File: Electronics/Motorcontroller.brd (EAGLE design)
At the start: 101.3 x 50.8 mm, 33 parts, among them Q1 IRFZ48V, Q2 IRF4905V, Q3 IRFZ48V, Q4 IRF4905V, Q5 IRFZ48V, Q6 IRF4905V, Q7 IRFZ48V, Q8 IRF4905V, X3 24V Batt

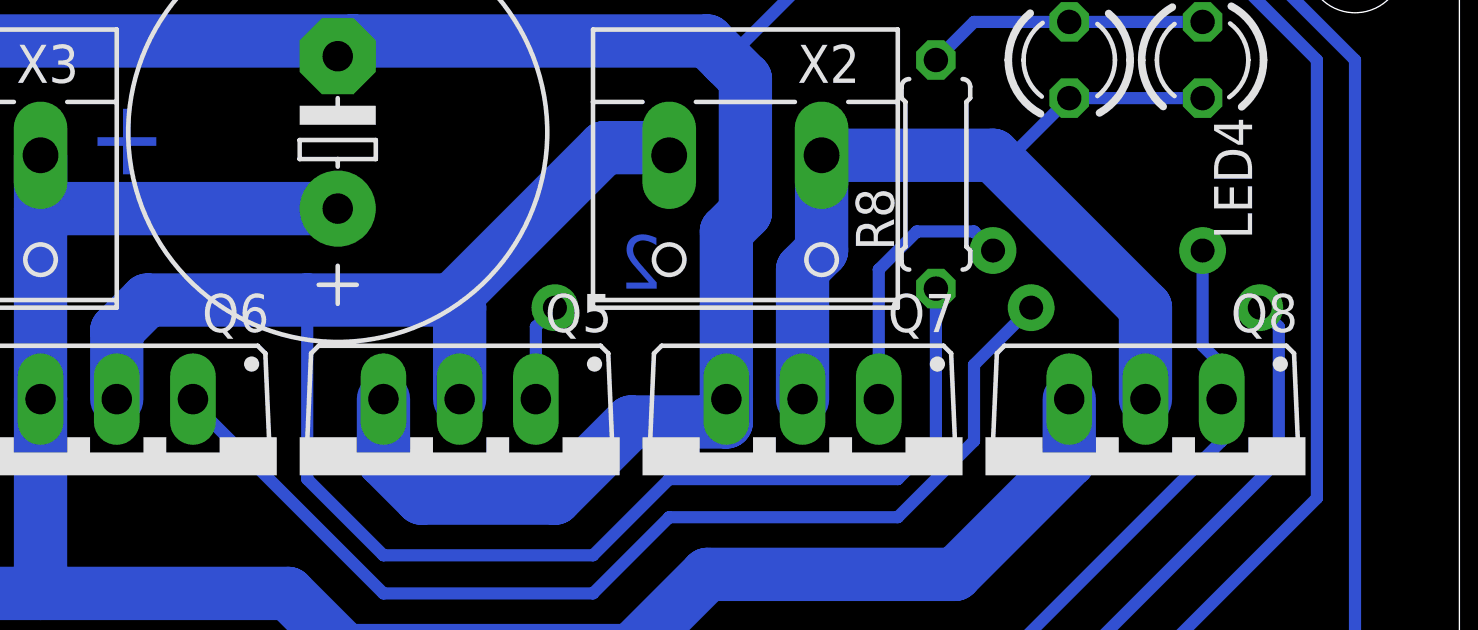
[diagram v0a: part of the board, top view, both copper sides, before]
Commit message: Renamed HEXFETs so both bridge fit
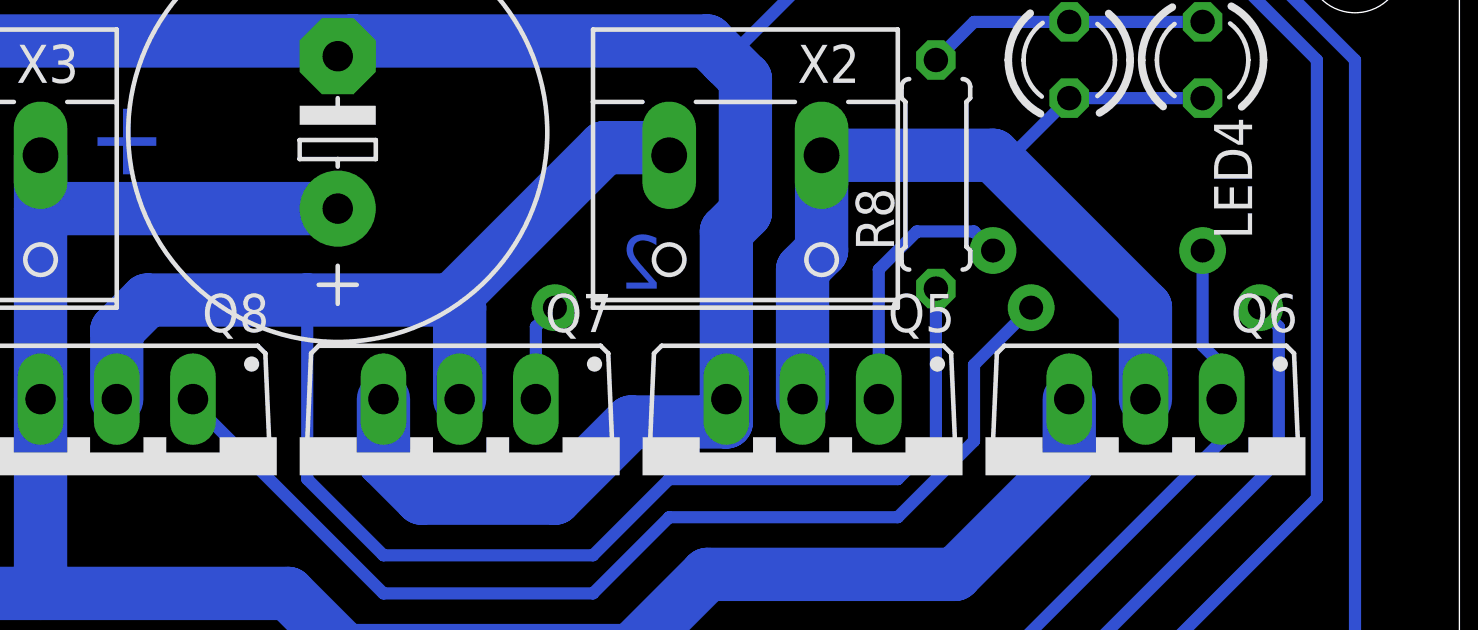
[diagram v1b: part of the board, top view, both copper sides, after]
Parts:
- moved Q6 34.3 mm to (90.2, 61.7)
- moved Q8 34.3 mm to (55.9, 61.7)
- moved Q5 11.4 mm to (78.7, 61.7)
- moved Q7 11.4 mm to (67.3, 61.7)
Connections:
- net N$1: now also Q5.D, Q6.D; no longer Q7.D, Q8.D
- net N$19: now also Q5.G, Q6.G; no longer Q7.G, Q8.G
- net N$21: now also Q8.G; no longer Q6.G
- net N$22: now also Q7.G; no longer Q5.G
- net N$25: now also Q7.D, Q8.D; no longer Q5.D, Q6.D
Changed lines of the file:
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@@
 <element name="R2" library="rcl" package="0207/10" value="10k" x="36.83" y="52.07" rot="R180"/>
 <element name="R3" library="rcl" package="0207/10" value="10k" x="50.8" y="52.07"/>
-<element name="Q5" library="transistor-power" package="TO220BV" value="IRFZ48V" x="67.31" y="61.722" rot="R180"/>
-<element name="Q6" library="transistor-power" package="TO220BV" value="IRF4905V" x="55.88" y="61.722" rot="R180"/>
+<element name="Q7" library="transistor-power" package="TO220BV" value="IRFZ48V" x="67.31" y="61.722" rot="R180"/>
+<element name="Q8" library="transistor-power" package="TO220BV" value="IRF4905V" x="55.88" y="61.722" rot="R180"/>
 <element name="X2" library="con-wago-508" package="W237-132" value="" x="76.835" y="71.755" rot="R180">
 <attribute name="OC_NEWARK" value="unknown" x="88.265" y="73.025" size="1.778" layer="27" rot="R180" display="off"/>
@@
 <attribute name="OC_FARNELL" value="unknown" x="88.265" y="73.025" size="1.778" layer="27" rot="R180" display="off"/>
 </element>
-<element name="Q7" library="transistor-power" package="TO220BV" value="IRFZ48V" x="78.74" y="61.722" rot="R180"/>
-<element name="Q8" library="transistor-power" package="TO220BV" value="IRF4905V" x="90.17" y="61.722" rot="R180"/>
+<element name="Q5" library="transistor-power" package="TO220BV" value="IRFZ48V" x="78.74" y="61.722" rot="R180"/>
+<element name="Q6" library="transistor-power" package="TO220BV" value="IRF4905V" x="90.17" y="61.722" rot="R180"/>
 <element name="R4" library="rcl" package="0207/10" value="10k" x="62.865" y="52.07" rot="R180"/>
 <element name="R5" library="rcl" package="0207/10" value="10k" x="75.565" y="52.07" rot="R180"/>
@@
 </signal>
 <signal name="N$19">
-<contactref element="Q8" pad="G"/>
-<contactref element="Q7" pad="G"/>
+<contactref element="Q6" pad="G"/>
+<contactref element="Q5" pad="G"/>
 <contactref element="R4" pad="1"/>
 <contactref element="OK4" pad="5"/>
@@
 </signal>
 <signal name="N$21">
-<contactref element="Q6" pad="G"/>
+<contactref element="Q8" pad="G"/>
 <contactref element="R5" pad="1"/>
 <contactref element="OK5" pad="5"/>
@@
 </signal>
 <signal name="N$22">
-<contactref element="Q5" pad="G"/>
+<contactref element="Q7" pad="G"/>
 <contactref element="R6" pad="1"/>
 <contactref element="OK6" pad="5"/>
@@
 </signal>
 <signal name="GND2">
+<contactref element="Q5" pad="S"/>
 <contactref element="Q7" pad="S"/>
-<contactref element="Q5" pad="S"/>
 <contactref element="X3" pad="2"/>
 <contactref element="Q3" pad="S"/>
@@
 <contactref element="Q4" pad="S"/>
 <contactref element="Q2" pad="S"/>
-<contactref element="Q6" pad="S"/>
+<contactref element="Q8" pad="S"/>
 <contactref element="R6" pad="2"/>
 <contactref element="R5" pad="2"/>
@@
 <contactref element="R2" pad="2"/>
 <contactref element="R1" pad="2"/>
-<contactref element="Q8" pad="S"/>
+<contactref element="Q6" pad="S"/>
 <contactref element="X3" pad="1"/>
 <wire x1="30.48" y1="64.262" x2="30.48" y2="60.96" width="1.778" layer="16"/>
@@
 </signal>
 <signal name="N$25">
-<contactref element="Q5" pad="D"/>
-<contactref element="Q6" pad="D"/>
+<contactref element="Q7" pad="D"/>
+<contactref element="Q8" pad="D"/>
 <contactref element="X2" pad="2"/>
 <wire x1="55.88" y1="64.262" x2="55.88" y2="66.548" width="1.778" layer="16"/>
@@
 <contactref element="LED4" pad="K"/>
 <contactref element="LED5" pad="A"/>
-<contactref element="Q8" pad="D"/>
-<contactref element="Q7" pad="D"/>
+<contactref element="Q6" pad="D"/>
+<contactref element="Q5" pad="D"/>
 <contactref element="X2" pad="1"/>
 <wire x1="78.74" y1="64.262" x2="78.74" y2="68.58" width="1.778" layer="16"/>

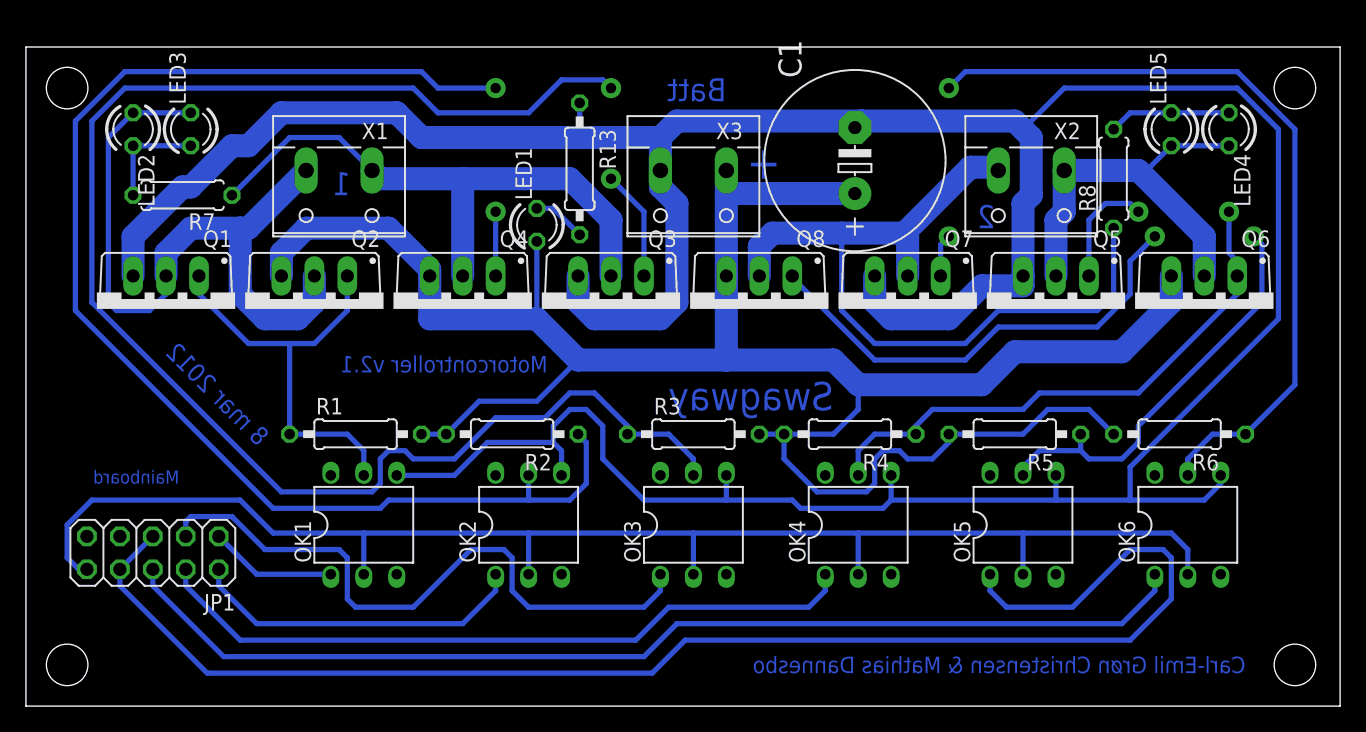
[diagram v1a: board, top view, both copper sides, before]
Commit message: Redesign of motorboard. Closes #30
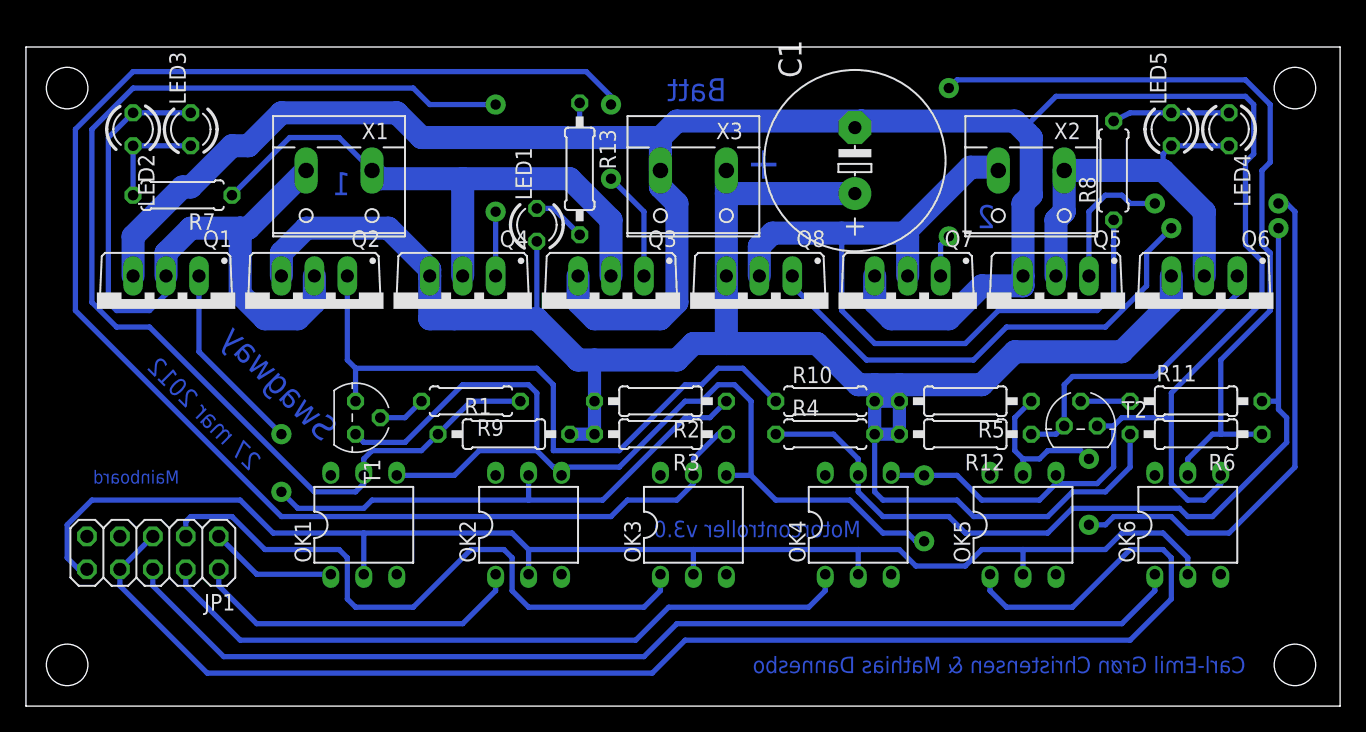
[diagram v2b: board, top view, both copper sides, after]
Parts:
- added R10, R9: 10k, rcl:0207/7
- added R11, R12: 10k, rcl:0207/10
- added T1, T2: BC547, transistor:TO92
- R4: device rcl:0207/10 -> rcl:0207/7
- moved R2 11.7 mm to (48.3, 54.6)
- moved R1 11.4 mm to (36.2, 52.1)
- moved R5 4.58 mm to (71.8, 54.6)
- moved R3 2.54 mm to (48.3, 52.1), turned to 180 degrees
- moved R4 1.91 mm to (61.0, 52.1), turned to 0 degrees
- moved R6 1.27 mm to (89.5, 52.1)
- moved R8 0.64 mm to (83.2, 72.4)
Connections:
- new net N$14: R9.2, T1.2
- new net N$15: Q2.G, R10.1, T1.3
- new net N$16: OK4.5, Q8.G, R11.2, R4.1
- new net N$18: R11.1, T2.2
- net +24V: now also R10.2, R12.2
- net GND2: now also T1.1, T2.1
- net N$12: now also Q4.G, R9.1; no longer Q1.G, Q2.G
- net N$19: now also R12.1, T2.3; no longer OK4.5, Q5.G, R4.1
- net N$21: now also Q5.G; no longer Q8.G
- net N$9: now also Q1.G; no longer Q4.G
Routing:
- net N$16: track 0.00 -> 103.5 mm, vias 0 -> 1
- net N$12: track 33.3 -> 94.3 mm
- net N$9: track 106.5 -> 54.8 mm, vias 2 -> 0
- net N$15: track 0.00 -> 51.6 mm
- net N$19: track 52.1 -> 23.6 mm, vias 2 -> 0
- net GND2: track 270.0 -> 296.1 mm
- net +24V: track 172.7 -> 162.3 mm
- net N$21: track 68.3 -> 62.9 mm, vias 2 -> 0
- net N$18: track 0.00 -> 3.81 mm
- net N$14: track 0.00 -> 3.70 mm
- net GND: track 110.9 -> 107.6 mm
- net N$13: track 126.6 -> 127.5 mm, vias 2 -> 1
- net N$25: track 61.3 -> 62.0 mm
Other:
- board text added: "27 mar 2012"
- board text added: "Motorcontroller v3.0"
- board text removed: "8 mar 2012"
- board text removed: "Motorcontroller v2.1"

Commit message: New motorcontroller with pull-down
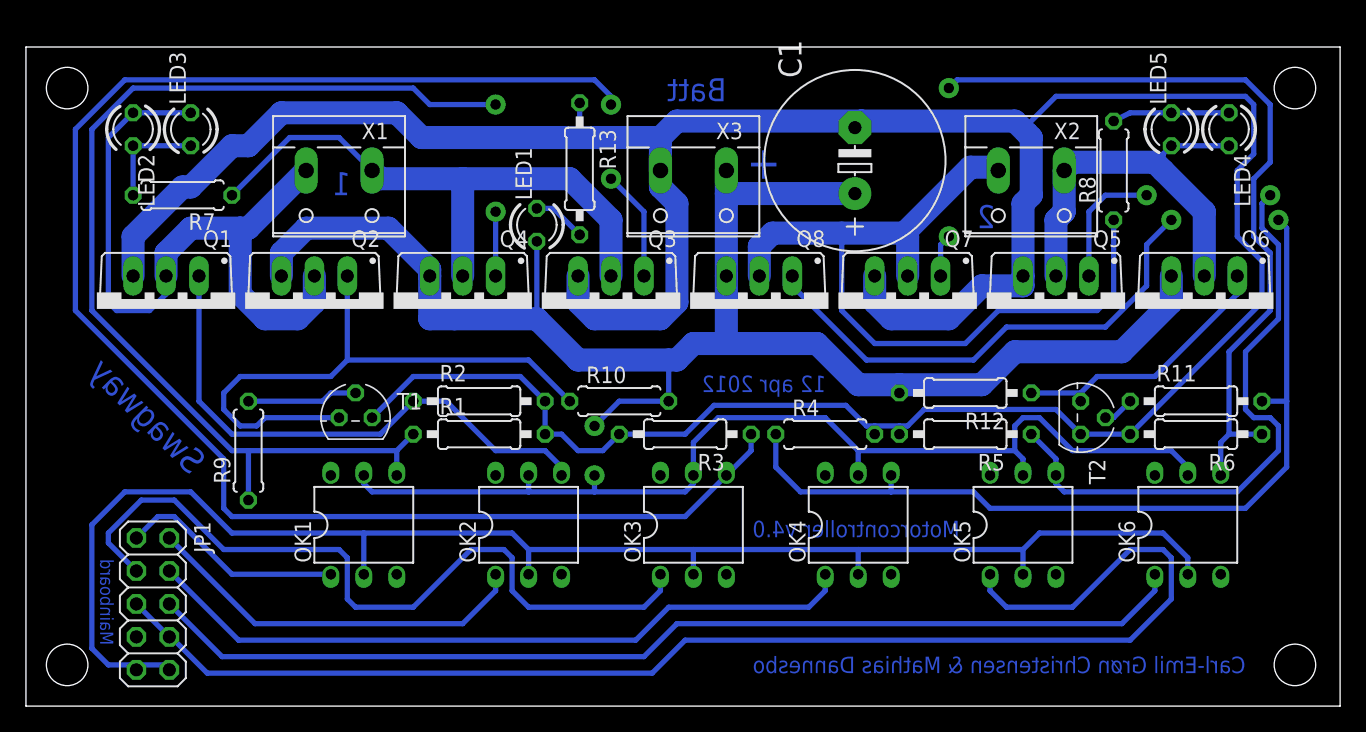
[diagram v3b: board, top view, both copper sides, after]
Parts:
- moved R9 17.6 mm to (16.5, 50.8), turned to 90 degrees
- moved R10 15.9 mm to (45.1, 54.6)
- moved R2 14.0 mm to (34.3, 54.6), turned to 0 degrees
- moved JP1 3.94 mm to (9.14, 39.0), turned to 270 degrees
- moved R12 3.17 mm to (71.8, 55.2)
- moved R5 2.54 mm to (71.8, 52.1)
- moved R1 1.91 mm to (34.3, 52.1)
- moved R3 1.91 mm to (50.2, 52.1)
- moved T2 0.64 mm to (80.6, 53.3), turned to 270 degrees
- turned T1 to 0 degrees
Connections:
- net +24V: now also OK1.5, OK2.5, OK3.5, OK4.5, OK5.5, OK6.5; no longer R1.2, R2.2, R3.2, R4.2, R5.2, R6.2
- net GND2: now also R1.2, R2.2, R3.2, R4.2, R5.2, R6.2; no longer OK1.4, OK2.4, OK3.4, OK4.4, OK5.4, OK6.4
- net N$12: now also OK1.4; no longer OK1.5
- net N$13: now also OK3.4; no longer OK3.5
- net N$16: now also OK4.4; no longer OK4.5
- net N$21: now also OK5.4; no longer OK5.5
- net N$22: now also OK6.4; no longer OK6.5
- net N$9: now also OK2.4; no longer OK2.5
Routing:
- net GND2: track 296.1 -> 251.9 mm
- net +24V: track 162.3 -> 205.2 mm, vias 0 -> 1
- net N$9: track 54.8 -> 42.4 mm
- net N$7: track 49.6 -> 59.7 mm
- net GND: track 107.6 -> 116.9 mm
- net N$3: track 9.85 -> 17.5 mm
- net N$12: track 94.3 -> 87.4 mm
- net N$10: track 112.1 -> 105.4 mm
- net N$21: track 62.9 -> 56.6 mm
- net N$15: track 51.6 -> 46.5 mm
- net N$14: track 3.70 -> 8.52 mm
- net N$5: track 26.1 -> 30.2 mm
- net N$13: track 127.5 -> 130.8 mm
- net N$11: track 84.1 -> 81.0 mm
- net N$19: track 23.6 -> 21.1 mm
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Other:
- board text added: "12 apr 2012"
- board text added: "Motorcontroller v4.0"
- board text removed: "27 mar 2012"
- board text removed: "Motorcontroller v3.0"

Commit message: Reroute and tidy-up. New version number
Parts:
- R1, R2, R3: device rcl:0207/10 -> rcl:0207/7
- R4: device rcl:0207/7 -> rcl:0207/10
- moved R1 17.2 mm to (17.1, 51.4), turned to 90 degrees
- moved LED1 8.76 mm to (41.3, 76.6), turned to 270 degrees
- moved R10 7.43 mm to (38.1, 52.1)
- moved R13 4.07 mm to (38.0, 72.3), turned to 90 degrees
- moved R2 3.81 mm to (38.1, 54.6), turned to 180 degrees
- moved R9 3.24 mm to (19.7, 51.4)
- moved R3 2.29 mm to (48.3, 53.3)
- moved R4 1.80 mm to (59.7, 53.3)
- moved R12 0.63 mm to (71.8, 54.6)
- moved T1 0.63 mm to (24.8, 54.0), turned to 90 degrees
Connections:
- net +24V: now also R13.1; no longer LED1.A
- net GND2: now also LED1.K; no longer R13.1
- net N$6: now also LED1.A; no longer LED1.K
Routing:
- net GND: track 116.9 -> 161.0 mm
- net N$15: track 46.5 -> 22.2 mm, vias 0 -> 1
- net N$21: track 56.6 -> 45.6 mm
- net N$7: track 59.7 -> 50.4 mm
- net GND2: track 251.9 -> 258.8 mm
- net N$14: track 8.52 -> 3.70 mm
- net N$9: track 42.4 -> 46.4 mm
- net N$16: track 105.7 -> 108.1 mm
- net +24V: track 205.2 -> 203.7 mm, vias 1 -> 0
- net N$5: track 30.2 -> 28.8 mm
- net N$11: track 81.0 -> 80.0 mm
- net N$8: track 55.6 -> 54.6 mm
- net N$10: track 105.4 -> 104.3 mm
- net N$12: track 87.4 -> 86.6 mm
- net N$13: track 130.8 -> 131.4 mm
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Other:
- board text added: "& Mathias Dannesbo"
- board text added: "13 apr 2012"
- board text added: "Carl-Emil Grøn Christensen"
- board text added: "Motorcontroller v4.1"
- board text removed: "12 apr 2012"
- board text removed: "Batt"
- board text removed: "Carl-Emil Grøn Christensen & Mathias Dannesbo"
- board text removed: "Motorcontroller v4.0"
